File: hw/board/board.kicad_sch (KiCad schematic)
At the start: 11 parts, among them J2 Conn_ARM_JTAG_SWD_10, U2 W25Q128JVSIQTR, U6 XC7A35T-FTG256

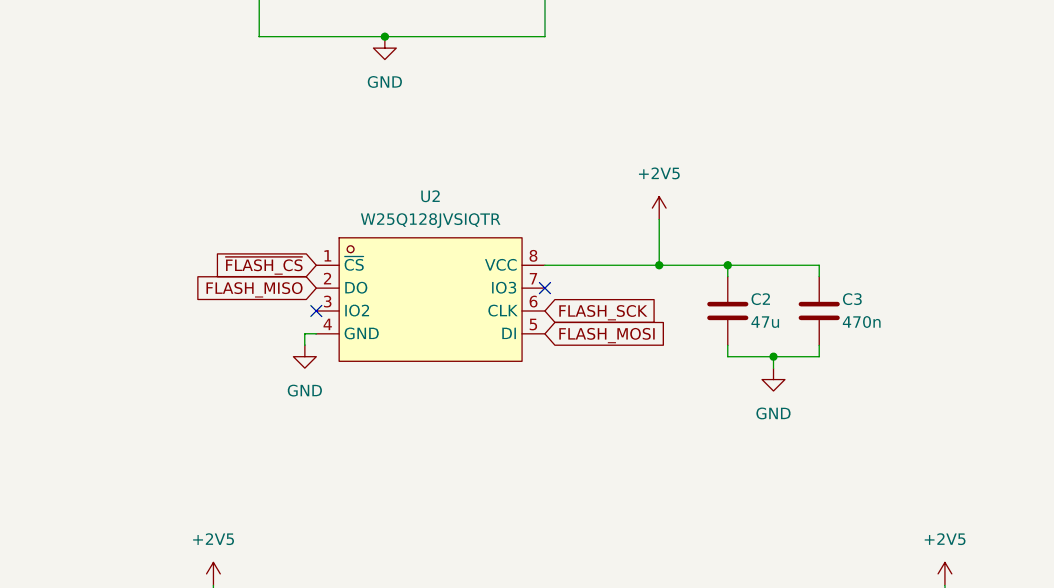
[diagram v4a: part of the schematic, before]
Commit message: Reduced flash size
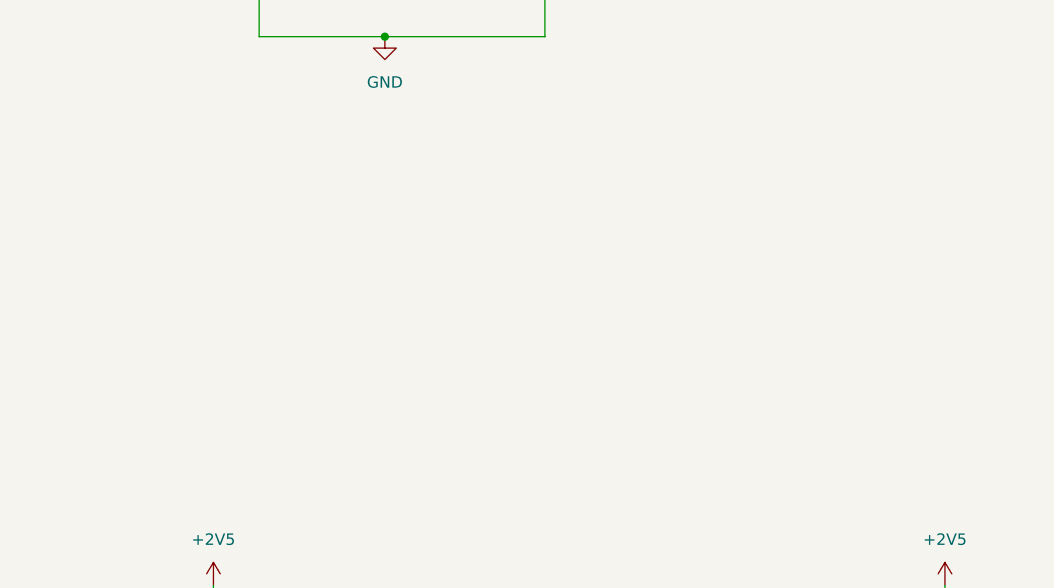
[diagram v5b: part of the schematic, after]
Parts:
- removed C2: 47u, Capacitor_SMD:C_0805_2012Metric, symbol Device:C
- removed C3: 470n, Capacitor_SMD:C_0805_2012Metric, symbol Device:C
- removed U2: W25Q128JVSIQTR, EasyEDA:SOIC-8_L5.3-W5.3-P1.27-LS8.0-BL, symbol EasyEDA:W25Q128JVSIQTR
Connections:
- no-connect marks 116 -> 114

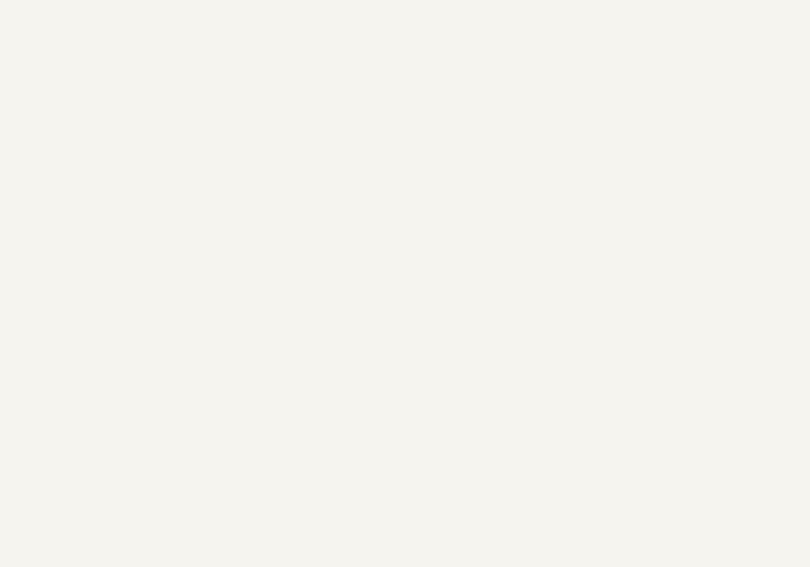
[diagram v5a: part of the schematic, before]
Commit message: Updated verilog to more closely match ECSS standard for encoding layer
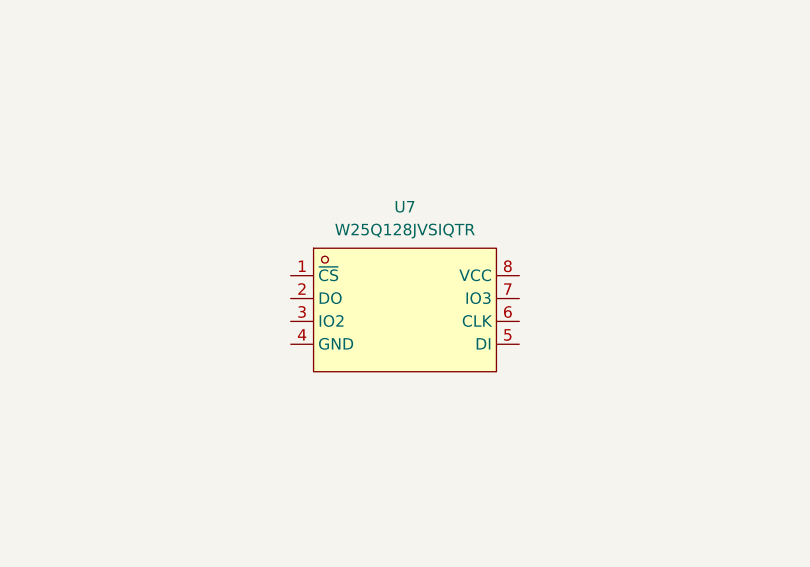
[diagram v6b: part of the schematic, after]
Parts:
- added U7: W25Q128JVSIQTR, EasyEDA:SOIC-8_L5.3-W5.3-P1.27-LS8.0-BL, symbol EasyEDA:W25Q128JVSIQTR
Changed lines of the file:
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@@
+	)
+	(symbol
+		(lib_id "EasyEDA:W25Q128JVSIQTR")
+		(at 215.9 259.08 0)
+		(unit 1)
+		(exclude_from_sim no)
+		(in_bom yes)
+		(on_board yes)
+		(dnp no)
+		(fields_autoplaced yes)
+		(property "Reference" "U7"
+			(at 215.9 247.65 0)
+			(effects
+				(font
+					(size 1.27 1.27)
+				)
+			)
+		)
+		(property "Value" "W25Q128JVSIQTR"
+			(at 215.9 250.19 0)
+			(effects
+				(font
+					(size 1.27 1.27)
+				)
+			)
+		)
+		(property "Footprint" "EasyEDA:SOIC-8_L5.3-W5.3-P1.27-LS8.0-BL"
+			(at 215.9 270.51 0)
+			(effects
+				(font
+					(size 1.27 1.27)
+				)
+				(hide yes)
+			)
+		)
+		(property "Datasheet" "https://lcsc.com/product-detail/FLASH_W25Q128JVSIQTR_C97521.html"
+			(at 215.9 273.05 0)
+			(effects
+				(font
+					(size 1.27 1.27)
+				)
+				(hide yes)
+			)
+		)
+		(property "Description" ""
+			(at 215.9 259.08 0)
+			(effects
+				(font
+					(size 1.27 1.27)
+				)
+				(hide yes)
+			)
+		)
+		(property "LCSC Part" "C97521"
+			(at 215.9 275.59 0)
+			(effects
+				(font
+					(size 1.27 1.27)
+				)
+				(hide yes)
+			)
+		)
+		(pin "3"
+		)
+		(pin "8"
+		)
+		(pin "2"
+		)
+		(pin "7"
+		)
+		(pin "6"
+		)
+		(pin "5"
+		)
+		(pin "4"
+		)
+		(pin "1"
+		)
+		(instances
+			(project ""
+				(path "/0e384709-6bce-4dbf-a0e0-550e970390f4"
+					(reference "U7")
+					(unit 1)
+				)
+			)
+		)
 	)
 	(symbol
